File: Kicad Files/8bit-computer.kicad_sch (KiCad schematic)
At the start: 26 parts

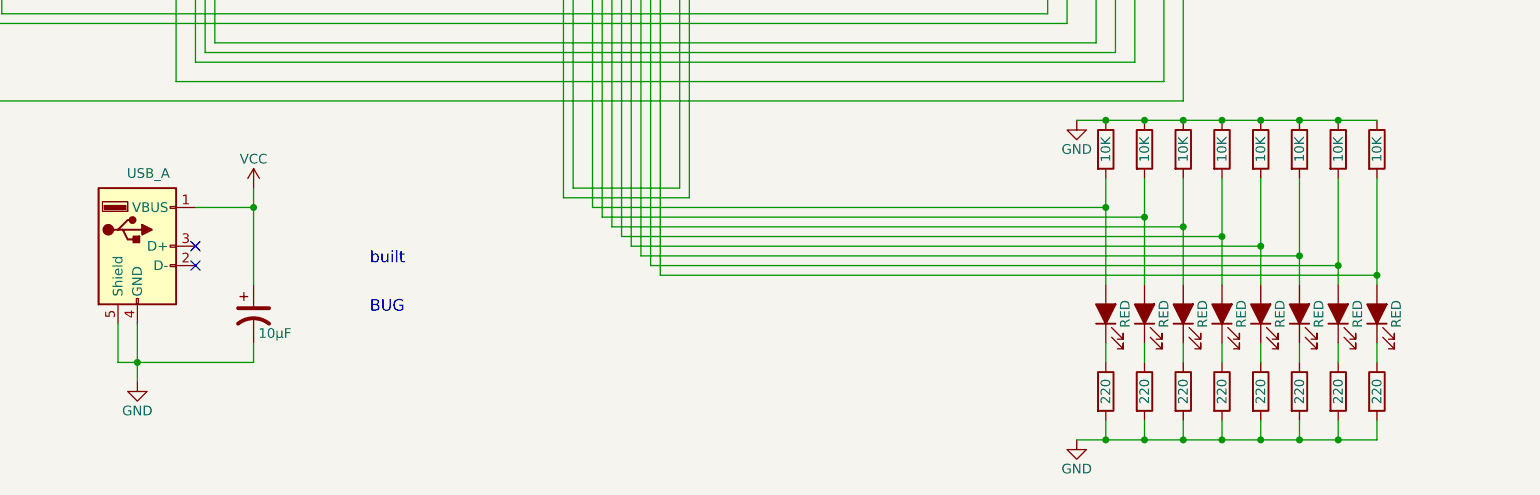
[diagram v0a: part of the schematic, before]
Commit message: started tidy up in control
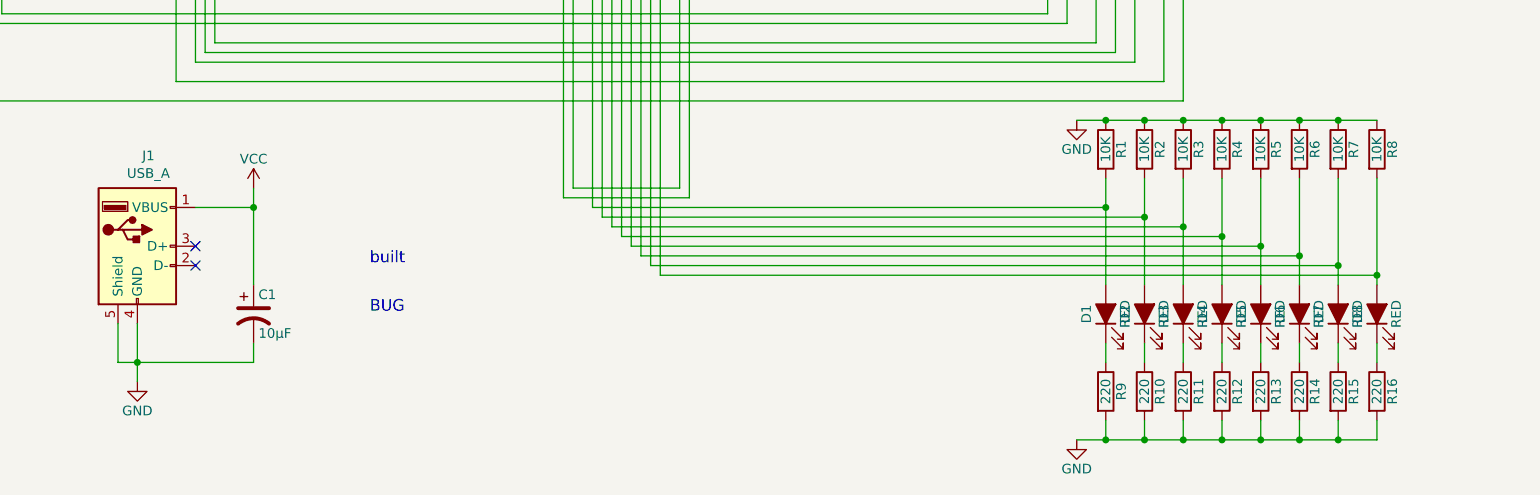
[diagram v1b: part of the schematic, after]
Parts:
- gave numbers to parts that had none: 26

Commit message: work on cl
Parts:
- R1: value 10K -> R
- R10: renamed from R13; value 220 -> R
- R11: renamed from R6; value 10K -> R
- R12: renamed from R14; value 220 -> R
- R13: renamed from R7; value 10K -> R
- R14: renamed from R15; value 220 -> R
- R15: renamed from R8; value 10K -> R
- R16: value 220 -> R
- R2: renamed from R9; value 220 -> R
- R3: renamed from R2; value 10K -> R
- R4: renamed from R10; value 220 -> R
- R5: renamed from R3; value 10K -> R
- R6: renamed from R11; value 220 -> R
- R7: renamed from R4; value 10K -> R
- R8: renamed from R12; value 220 -> R
- R9: renamed from R5; value 10K -> R
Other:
- moved on the sheet: D1, D2, D3, D4, D5, D6, D7, D8, R1, R10, R11, R12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

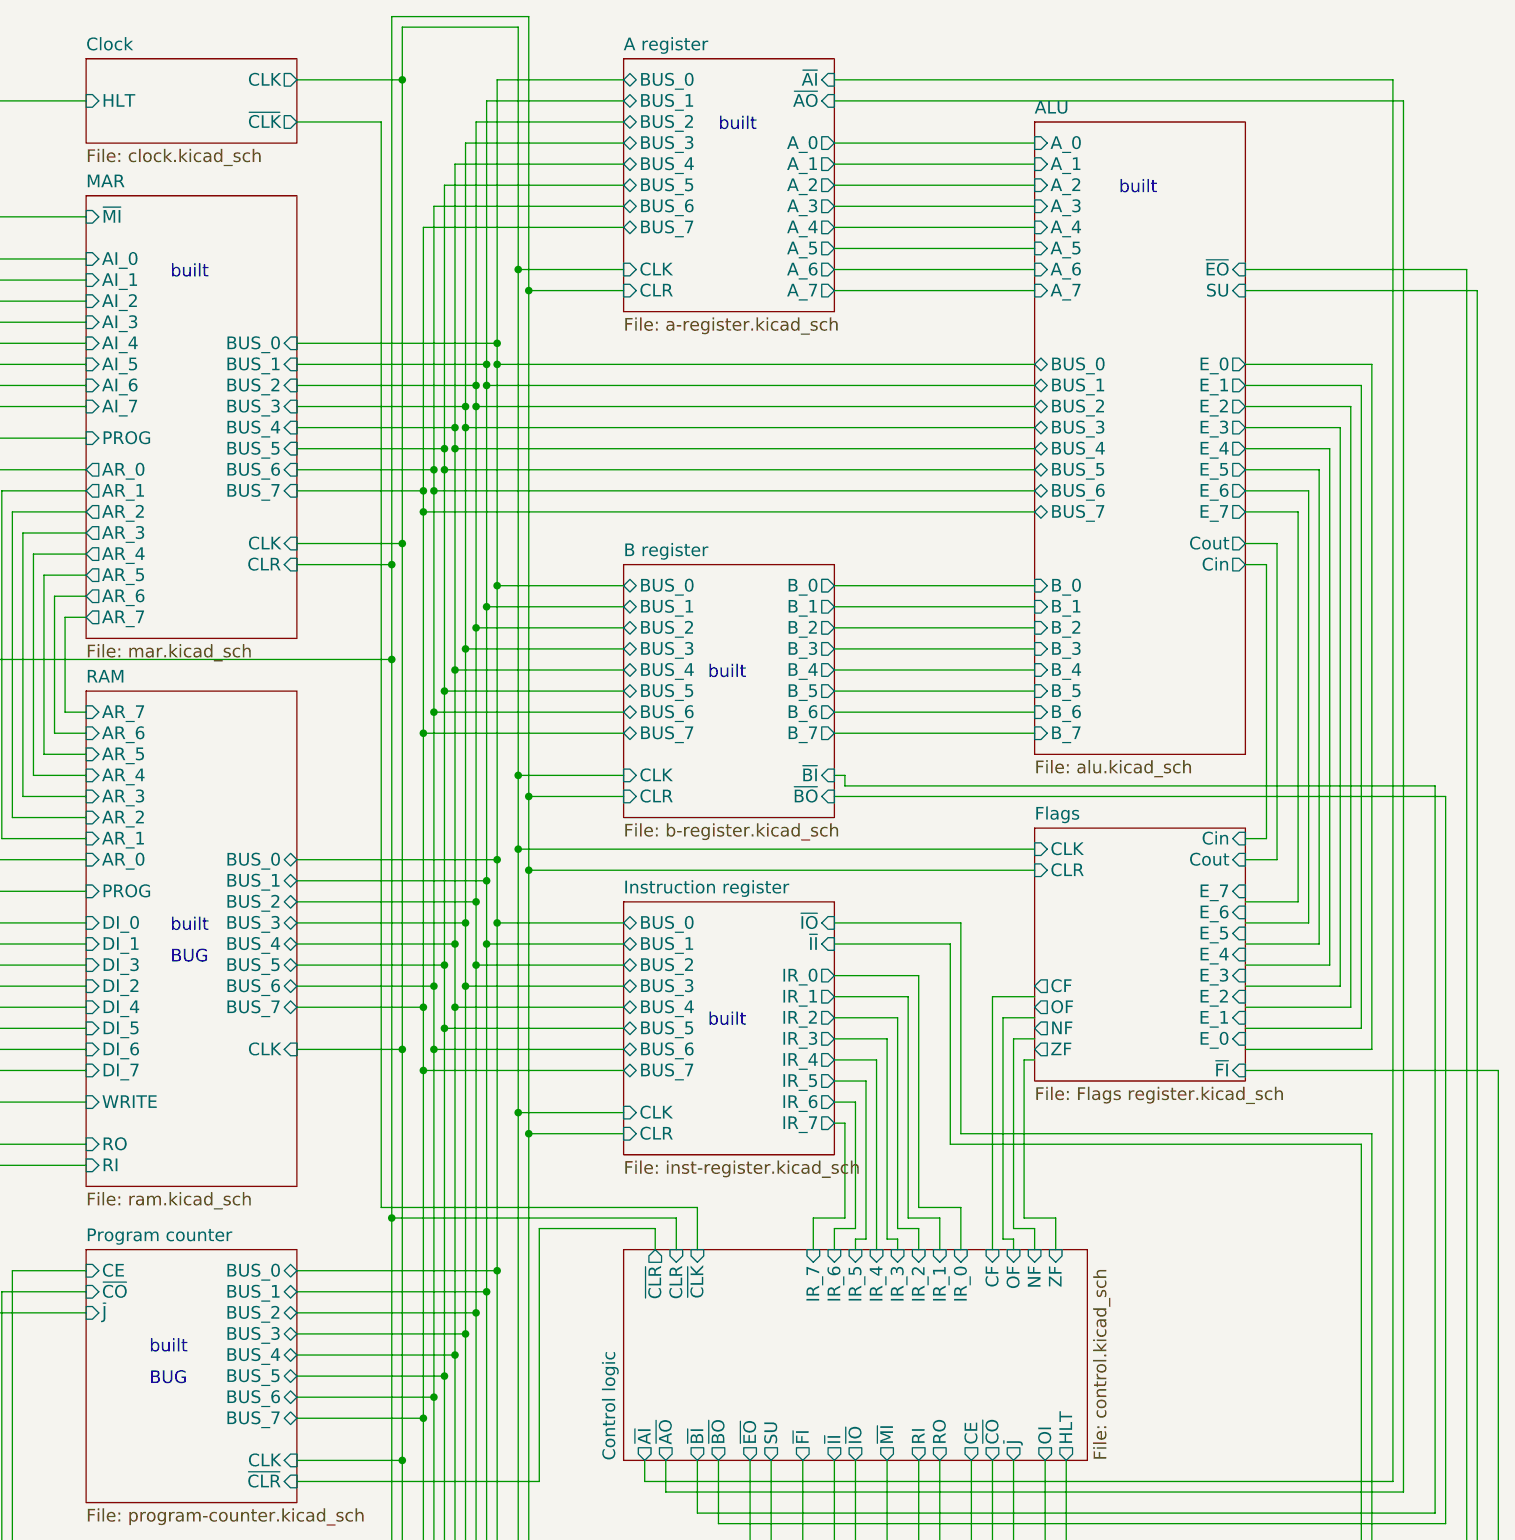
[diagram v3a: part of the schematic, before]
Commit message: fixed ecc problems
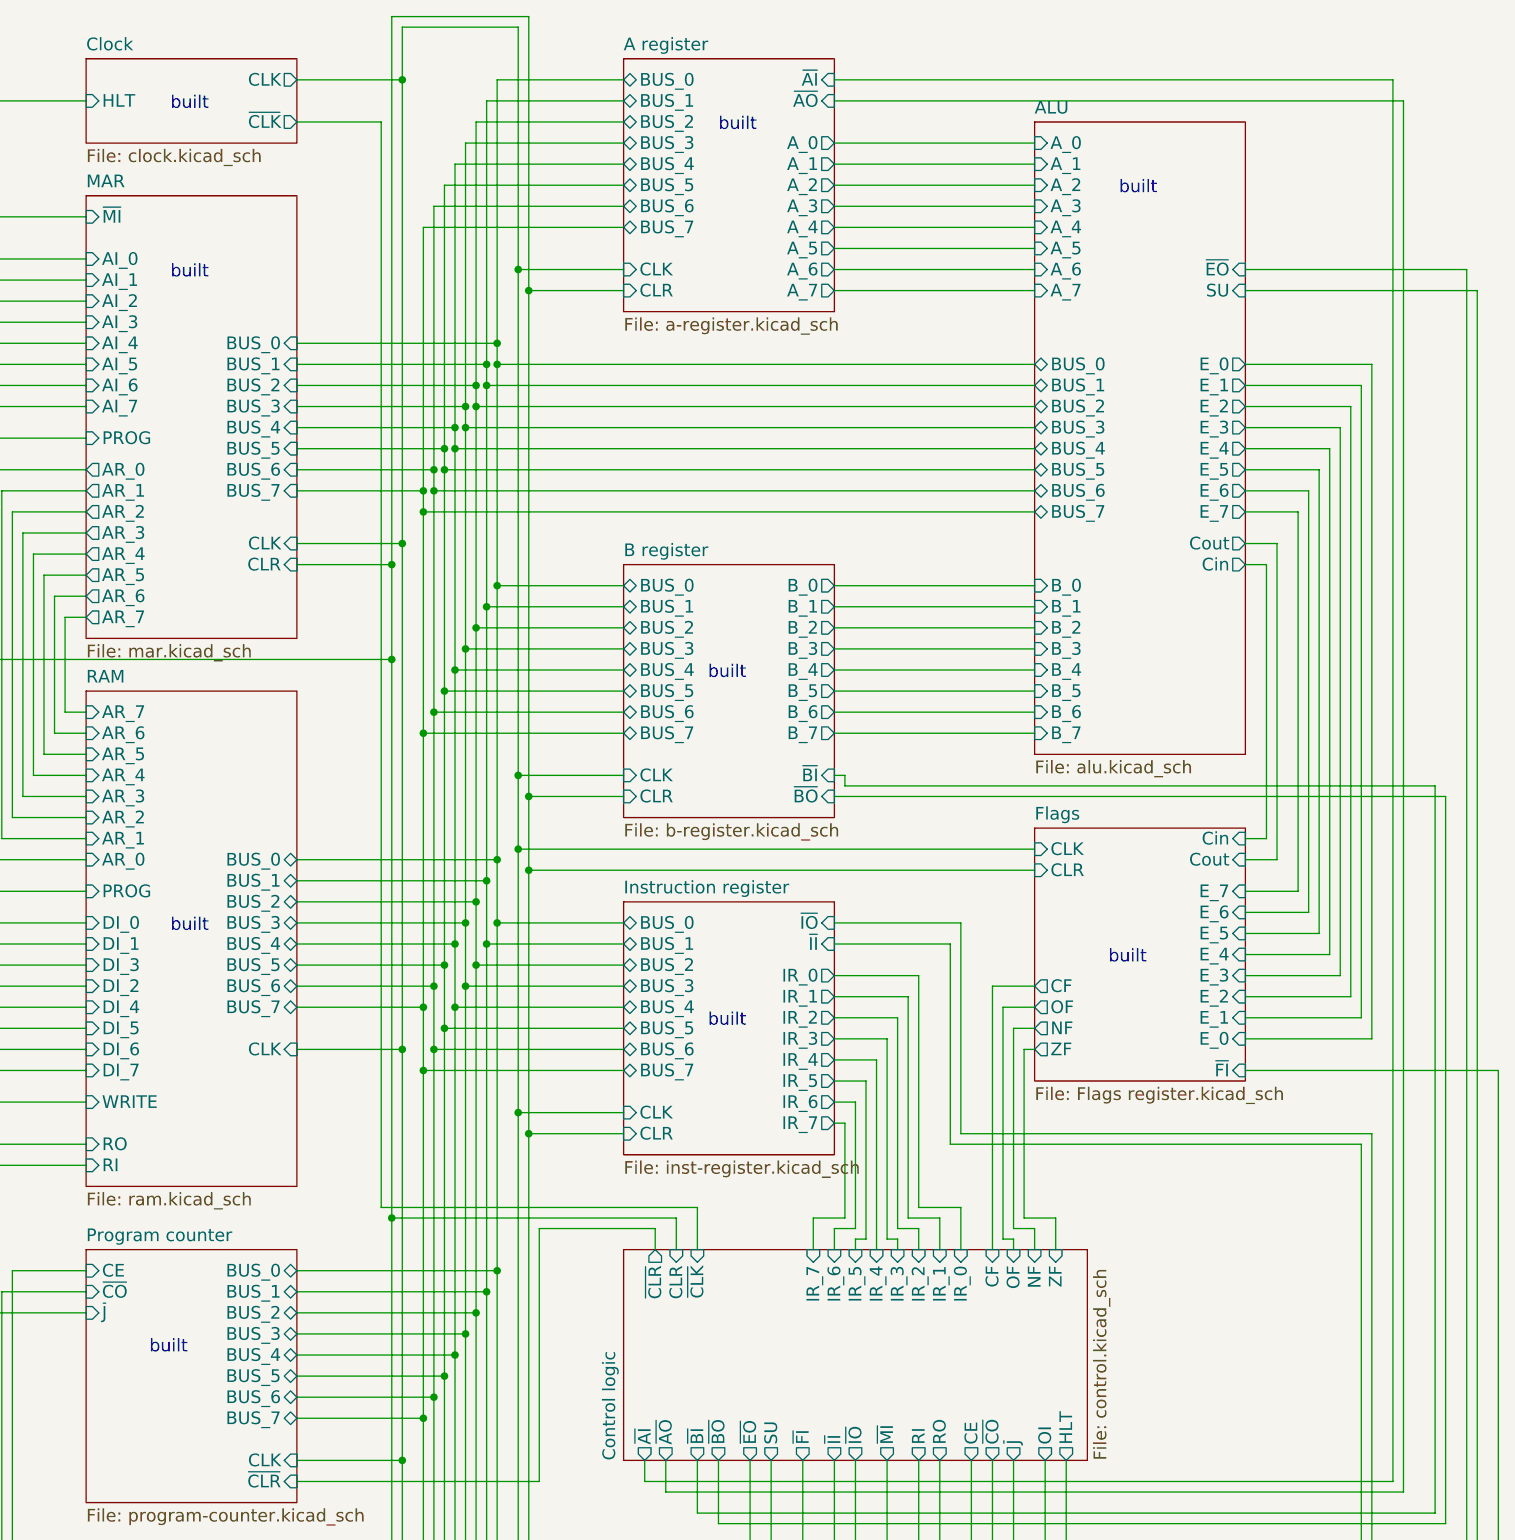
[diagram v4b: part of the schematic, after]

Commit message: changed to 16bit Addr Bus
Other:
- added sheet X register (x-register.kicad_sch)
- sheet MAR ports: added AR_00, AR_01, AR_02, AR_03, AR_04, AR_05, AR_06, AR_07, AR_08, AR_09, AR_10, AR_11, AR_12, AR_13, AR_14, AR_15, MO, ~{MIhb}, ~{MIlb}; removed AI_0, AI_1, AI_2, AI_3, AI_4, AI_5, AI_6, AI_7, AR_0, AR_1, AR_2, AR_3, AR_4, AR_5, AR_6, AR_7, PROG, ~{MI}
- sheet RAM ports: added AR_00, AR_01, AR_02, AR_03, AR_04, AR_05, AR_06, AR_07, AR_08, AR_09, AR_10, AR_11, AR_12, AR_13, AR_14, AR_15; removed AR_0, AR_1, AR_2, AR_3, AR_4, AR_5, AR_6, AR_7, DI_0, DI_1, DI_2, DI_3, DI_4, DI_5, DI_6, DI_7
- note added: "TODO: redraw regs redraw ic connect mar,xreg control sigs"
- moved on the sheet: C1, J1

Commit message: w1
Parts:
- removed D1, D2, D3, D4, D5, D6, D7, D8: RED, LED_THT:LED_D5.0mm, symbol 8bit-computer-rescue:LED_ALT-Device
- removed R1, R10, R11, R12, R13, R14, R15, R16, R2, R3, R4, R5, R6, R7, R8, R9: R, Resistor_THT:R_Axial_DIN0207_L6.3mm_D2.5mm_P7.62mm_Horizontal, symbol Device:R
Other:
- sheet MAR ports: added ABUS_00, ABUS_01, ABUS_02, ABUS_03, ABUS_04, ABUS_05, ABUS_06, ABUS_07, ABUS_08, ABUS_09, ABUS_10, ABUS_11, ABUS_12, ABUS_13, ABUS_14, ABUS_15; removed AR_00, AR_01, AR_02, AR_03, AR_04, AR_05, AR_06, AR_07, AR_08, AR_09, AR_10, AR_11, AR_12, AR_13, AR_14, AR_15
- sheet RAM ports: added ABUS_00, ABUS_01, ABUS_02, ABUS_03, ABUS_04, ABUS_05, ABUS_06, ABUS_07, ABUS_08, ABUS_09, ABUS_10, ABUS_11, ABUS_12, ABUS_13, ABUS_14, ABUS_15; removed AR_00, AR_01, AR_02, AR_03, AR_04, AR_05, AR_06, AR_07, AR_08, AR_09, AR_10, AR_11, AR_12, AR_13, AR_14, AR_15
- note added: "TODO: redraw ic connect mar,xreg control sigs rework pc to 16bit"
- note removed: "TODO: redraw regs redraw ic connect mar,xreg control sigs"
- moved on the sheet: C1, J1

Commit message: w2
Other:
- note added: "TODO: redraw ic connect mar,xreg control sigs rework pc to 16bit(control sigs)"
- note removed: "TODO: redraw ic connect mar,xreg control sigs rework pc to 16bit"
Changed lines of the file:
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@@
     (effects (font (size 1.524 1.524)) (justify left bottom))
   )
-  (text "TODO:\n\nredraw ic\nconnect mar,xreg control sigs\nrework pc to 16bit\n\n"
+  (text "TODO:\n\nredraw ic\nconnect mar,xreg control sigs\nrework pc to 16bit(control sigs)\n\n"
     (at 20.32 29.21 0)
     (effects (font (size 1.524 1.524)) (justify left bottom))
@@
       (reference "#PWR092") (unit 1) (value "GND") (footprint "")
     )
-    (path "/00000000-0000-0000-0000-00005b57994f/00000000-0000-0000-0000-00005b664c46"
-      (reference "#PWR093") (unit 1) (value "GND") (footprint "")
-    )
     (path "/00000000-0000-0000-0000-00005b57994f/00000000-0000-0000-0000-000061b29697"
       (reference "#PWR094") (unit 1) (value "VCC") (footprint "")
@@
       (reference "#PWR?") (unit 1) (value "VCC") (footprint "")
     )
+    (path "/00000000-0000-0000-0000-00005b57994f/5a198f69-af39-4aa1-b661-537da9b05752"
+      (reference "#PWR?") (unit 1) (value "VCC") (footprint "")
+    )
+    (path "/00000000-0000-0000-0000-00005b57994f/60f2c332-313d-48e5-b224-b98fa4b6f4be"
+      (reference "#PWR?") (unit 1) (value "GND") (footprint "")
+    )
     (path "/00000000-0000-0000-0000-00005b55f546/75e98ea8-7557-4e31-afd8-02186a0d1542"
       (reference "#PWR?") (unit 1) (value "GND") (footprint "")
@@
       (reference "#PWR?") (unit 1) (value "VCC") (footprint "")
     )
+    (path "/00000000-0000-0000-0000-00005b57994f/86b858c9-b19f-48d3-8325-10c689de92e3"
+      (reference "#PWR?") (unit 1) (value "VCC") (footprint "")
+    )
+    (path "/00000000-0000-0000-0000-00005b57994f/99087e1e-5666-4d76-be11-12f350764b38"
+      (reference "#PWR?") (unit 1) (value "VCC") (footprint "")
+    )
     (path "/240eb373-711e-4b1f-862f-22396c0693f9/9988e873-8929-484e-9285-17521cee5418"
       (reference "#PWR?") (unit 1) (value "GND") (footprint "")
@@
       (reference "#PWR?") (unit 1) (value "GND") (footprint "")
     )
+    (path "/00000000-0000-0000-0000-00005b57994f/b250f3e5-f1ae-4952-89e5-d486994182f1"
+      (reference "#PWR?") (unit 1) (value "GND") (footprint "")
+    )
     (path "/00000000-0000-0000-0000-00005b55f546/c2d89373-b429-4d66-9948-48461c8ff3fe"
       (reference "#PWR?") (unit 1) (value "VCC") (footprint "")
@@
       (reference "#PWR?") (unit 1) (value "GND") (footprint "")
     )
+    (path "/00000000-0000-0000-0000-00005b57994f/e1c54cf5-c290-497e-ab52-a5da62884a4e"
+      (reference "#PWR?") (unit 1) (value "VCC") (footprint "")
+    )
+    (path "/00000000-0000-0000-0000-00005b57994f/fc864c09-6ecf-4df0-ad34-444cc8fa7f3f"
+      (reference "#PWR?") (unit 1) (value "GND") (footprint "")
+    )
     (path "/00000000-0000-0000-0000-00006445a396/00000000-0000-0000-0000-00006470ddd3"
       (reference "A1") (unit 1) (value "Arduino_Nano_Every") (footprint "Module:Arduino_Nano")
@@
       (reference "D31") (unit 1) (value "RED") (footprint "LED_THT:LED_D5.0mm")
     )
-    (path "/00000000-0000-0000-0000-00005b57994f/00000000-0000-0000-0000-00005b664724"
-      (reference "D32") (unit 1) (value "GREEN") (footprint "LED_THT:LED_D5.0mm")
-    )
-    (path "/00000000-0000-0000-0000-00005b57994f/00000000-0000-0000-0000-00005b664702"
-      (reference "D33") (unit 1) (value "GREEN") (footprint "LED_THT:LED_D5.0mm")
-    )
-    (path "/00000000-0000-0000-0000-00005b57994f/00000000-0000-0000-0000-00005b664698"
-      (reference "D34") (unit 1) (value "GREEN") (footprint "LED_THT:LED_D5.0mm")
-    )
-    (path "/00000000-0000-0000-0000-00005b57994f/00000000-0000-0000-0000-00005b66460b"
-      (reference "D35") (unit 1) (value "GREEN") (footprint "LED_THT:LED_D5.0mm")
-    )
-    (path "/00000000-0000-0000-0000-00005b57994f/00000000-0000-0000-0000-000061da4ec7"
-      (reference "D36") (unit 1) (value "GREEN") (footprint "LED_THT:LED_D5.0mm")
-    )
-    (path "/00000000-0000-0000-0000-00005b57994f/00000000-0000-0000-0000-000061da4ebd"
-      (reference "D37") (unit 1) (value "GREEN") (footprint "LED_THT:LED_D5.0mm")
-    )
-    (path "/00000000-0000-0000-0000-00005b57994f/00000000-0000-0000-0000-000061da4eb3"
-      (reference "D38") (unit 1) (value "GREEN") (footprint "LED_THT:LED_D5.0mm")
-    )
-    (path "/00000000-0000-0000-0000-00005b57994f/00000000-0000-0000-0000-000061da4d77"
-      (reference "D39") (unit 1) (value "GREEN") (footprint "LED_THT:LED_D5.0mm")
-    )
     (path "/00000000-0000-0000-0000-00005b57d8e5/00000000-0000-0000-0000-00006193b54d"
       (reference "D40") (unit 1) (value "LED") (footprint "")
@@
       (reference "R62") (unit 1) (value "R") (footprint "Resistor_THT:R_Axial_DIN0207_L6.3mm_D2.5mm_P7.62mm_Horizontal")
     )
-    (path "/00000000-0000-0000-0000-00005b57994f/00000000-0000-0000-0000-00005b664abb"
-      (reference "R63") (unit 1) (value "R") (footprint "Resistor_THT:R_Axial_DIN0207_L6.3mm_D2.5mm_P7.62mm_Horizontal")
-    )
-    (path "/00000000-0000-0000-0000-00005b57994f/00000000-0000-0000-0000-00005b664a8d"
-      (reference "R64") (unit 1) (value "R") (footprint "Resistor_THT:R_Axial_DIN0207_L6.3mm_D2.5mm_P7.62mm_Horizontal")
-    )
-    (path "/00000000-0000-0000-0000-00005b57994f/00000000-0000-0000-0000-00005b664a62"
-      (reference "R65") (unit 1) (value "R") (footprint "Resistor_THT:R_Axial_DIN0207_L6.3mm_D2.5mm_P7.62mm_Horizontal")
-    )
-    (path "/00000000-0000-0000-0000-00005b57994f/00000000-0000-0000-0000-00005b664a10"
-      (reference "R66") (unit 1) (value "R") (footprint "Resistor_THT:R_Axial_DIN0207_L6.3mm_D2.5mm_P7.62mm_Horizontal")
-    )
-    (path "/00000000-0000-0000-0000-00005b57994f/00000000-0000-0000-0000-000061da4eef"
-      (reference "R67") (unit 1) (value "R") (footprint "Resistor_THT:R_Axial_DIN0207_L6.3mm_D2.5mm_P7.62mm_Horizontal")
-    )
-    (path "/00000000-0000-0000-0000-00005b57994f/00000000-0000-0000-0000-000061da4ee5"
-      (reference "R68") (unit 1) (value "R") (footprint "Resistor_THT:R_Axial_DIN0207_L6.3mm_D2.5mm_P7.62mm_Horizontal")
-    )
-    (path "/00000000-0000-0000-0000-00005b57994f/00000000-0000-0000-0000-000061da4edb"
-      (reference "R69") (unit 1) (value "R") (footprint "Resistor_THT:R_Axial_DIN0207_L6.3mm_D2.5mm_P7.62mm_Horizontal")
-    )
-    (path "/00000000-0000-0000-0000-00005b57994f/00000000-0000-0000-0000-000061da4ed1"
-      (reference "R70") (unit 1) (value "R") (footprint "Resistor_THT:R_Axial_DIN0207_L6.3mm_D2.5mm_P7.62mm_Horizontal")
-    )
     (path "/00000000-0000-0000-0000-00005b57d8e5/00000000-0000-0000-0000-00005b57e361"
       (reference "R71") (unit 1) (value "R") (footprint "Resistor_THT:R_Axial_DIN0207_L6.3mm_D2.5mm_P7.62mm_Horizontal")
@@
       (reference "U?") (unit 1) (value "74LS245") (footprint "Package_DIP:DIP-20_W7.62mm")
     )
+    (path "/00000000-0000-0000-0000-00005b57994f/7a1d1b5c-932e-47a3-9e1f-226fe4cc77aa"
+      (reference "U?") (unit 1) (value "74LS161") (footprint "")
+    )
+    (path "/00000000-0000-0000-0000-00005b57994f/9e6316e1-b1af-4ace-bd4e-417b150c0946"
+      (reference "U?") (unit 1) (value "74LS161") (footprint "")
+    )
+    (path "/00000000-0000-0000-0000-00005b57994f/a75557ad-cfac-40b4-9cfe-eb062c23df76"
+      (reference "U?") (unit 1) (value "74LS245") (footprint "")
+    )
     (path "/00000000-0000-0000-0000-00005b55f546/b6e46e4c-3990-45cd-bf79-1ff3ad7926b6"
